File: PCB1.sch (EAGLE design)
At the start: 312 parts, among them SW1 CT10-XXXX-A2, SW10 CT10-XXXX-A2, SW100 CT10-XXXX-A2, SW101 CT10-XXXX-A2, SW102 CT10-XXXX-A2, SW103 CT10-XXXX-A2, SW104 CT10-XXXX-A2, SW105 CT10-XXXX-A2, SW106 CT10-XXXX-A2, SW107 CT10-XXXX-A2, SW108 CT10-XXXX-A2, SW109 CT10-XXXX-A2, SW11 CT10-XXXX-A2, SW110 CT10-XXXX-A2, SW111 CT10-XXXX-A2, SW112 CT10-XXXX-A2, SW113 CT10-XXXX-A2, SW114 CT10-XXXX-A2, SW115 CT10-XXXX-A2, SW116 CT10-XXXX-A2, SW117 CT10-XXXX-A2, SW118 CT10-XXXX-A2, SW119 CT10-XXXX-A2, SW12 CT10-XXXX-A2, SW120 CT10-XXXX-A2, SW121 CT10-XXXX-A2, SW122 CT10-XXXX-A2, SW123 CT10-XXXX-A2, SW124 CT10-XXXX-A2, SW125 CT10-XXXX-A2, SW126 CT10-XXXX-A2, SW127 CT10-XXXX-A2, SW128 CT10-XXXX-A2, SW129 CT10-XXXX-A2, SW13 CT10-XXXX-A2, SW130 CT10-XXXX-A2, SW131 CT10-XXXX-A2, SW132 CT10-XXXX-A2, SW14 CT10-XXXX-A2, SW15 CT10-XXXX-A2, SW16 CT10-XXXX-A2, SW17 CT10-XXXX-A2, SW18 CT10-XXXX-A2, SW19 CT10-XXXX-A2, SW2 CT10-XXXX-A2, SW20 CT10-XXXX-A2, SW21 CT10-XXXX-A2, SW22 CT10-XXXX-A2, SW23 CT10-XXXX-A2, SW24 CT10-XXXX-A2, SW25 CT10-XXXX-A2, SW26 CT10-XXXX-A2, SW27 CT10-XXXX-A2, SW28 CT10-XXXX-A2, SW29 CT10-XXXX-A2, SW3 CT10-XXXX-A2, SW30 CT10-XXXX-A2, SW31 CT10-XXXX-A2, SW32 CT10-XXXX-A2, SW33 CT10-XXXX-A2, SW34 CT10-XXXX-A2, SW35 CT10-XXXX-A2, SW36 CT10-XXXX-A2, SW37 CT10-XXXX-A2, SW38 CT10-XXXX-A2, SW39 CT10-XXXX-A2, SW4 CT10-XXXX-A2, SW40 CT10-XXXX-A2, SW41 CT10-XXXX-A2, SW42 CT10-XXXX-A2, SW43 CT10-XXXX-A2, SW44 CT10-XXXX-A2, SW45 CT10-XXXX-A2, SW46 CT10-XXXX-A2, SW47 CT10-XXXX-A2, SW48 CT10-XXXX-A2, SW49 CT10-XXXX-A2, SW5 CT10-XXXX-A2, SW50 CT10-XXXX-A2, SW51 CT10-XXXX-A2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

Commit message: updated schematic to include oscillator, resistor packages, and split main schematic into the five PCBs that we will need. Also started the PCB3 layout that includes the microcontroller.
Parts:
- removed C1, C2, C3, C4, C5, C6, C7: (no value), rcl:C-USC0805
- removed ICSP: (no value), pinhead:PINHD-2X3
- removed JP1, JP2, JP3, JP4: (no value), pinhead:PINHD-1X25
- removed LED100, LED101, LED102, LED103, LED104, LED105, LED106, LED107, LED108, LED109, LED110, LED111, LED112, LED113, LED114, LED115, LED116, LED117, LED118, LED119, LED120, LED121, LED122, LED123, LED124, LED125, LED126, LED127, LED128, LED129, LED130, LED131, LED132, LED133, LED134, LED135, LED136, LED137, LED138, LED139, LED20, LED21, LED22, LED23, LED24, LED25, LED32, LED33, LED34, LED35, LED36, LED37, LED38, LED39, LED40, LED41, LED42, LED43, LED44, LED45, LED46, LED47, LED48, LED49, LED50, LED51, LED52, LED53, LED54, LED55, LED56, LED57, LED58, LED59, LED60, LED61, LED62, LED63, LED64, LED65, LED66, LED67, LED68, LED69, LED70, LED71, LED72, LED73, LED74, LED75, LED76, LED77, LED78, LED79, LED80, LED81, LED82, LED83, LED84, LED85, LED86, LED87, LED88, LED89, LED90, LED91, LED92, LED93, LED94, LED95, LED96, LED97, LED98, LED99: (no value), led:LEDSMT1206
- removed SW1, SW10, SW100, SW101, SW102, SW103, SW104, SW105, SW106, SW107, SW108, SW109, SW11, SW110, SW111, SW112, SW113, SW114, SW115, SW116, SW117, SW118, SW119, SW12, SW120, SW121, SW122, SW123, SW124, SW125, SW126, SW127, SW128, SW129, SW13, SW130, SW131, SW132, SW14, SW15, SW16, SW17, SW18, SW19, SW2, SW20, SW21, SW22, SW23, SW24, SW25, SW26, SW27, SW28, SW29, SW3, SW30, SW31, SW32, SW33, SW34, SW35, SW36, SW37, SW38, SW39, SW4, SW40, SW41, SW42, SW43, SW44, SW45, SW46, SW47, SW48, SW49, SW5, SW50, SW51, SW52, SW53, SW54, SW55, SW56, SW57, SW58, SW59, SW6, SW60, SW61, SW62, SW63, SW64, SW65, SW66, SW67, SW68, SW69, SW7, SW70, SW71, SW72, SW73, SW74, SW75, SW76, SW77, SW78, SW79, SW8, SW80, SW81, SW82, SW83, SW84, SW85, SW86, SW87, SW88, SW89, SW9, SW90, SW91, SW92, SW93, SW94, SW95, SW96, SW97, SW98, SW99: CT10-XXXX-A2, switch-coto:CT10-XXXX-A2
- removed U$10, U$11, U$12, U$13, U$14, U$15, U$16, U$17, U$18, U$19, U$20, U$21, U$22, U$23, U$24, U$25, U$6, U$7, U$8, U$9: MM74HC595TSSOP-LD16, ECE477_Guitutar:MM74HC595TSSOP-LD16
- added R4, R5: (no value), resistor-bourns:4814P-T01
- R1, R2: device rcl:R-US_M0805 -> resistor-bourns:4814P-T01
- U$1: value PIC32MX570F512L -> MM74HC595TSSOP-LD16; device PICMX5xx:PIC32MX570F512L -> ECE477_Guitutar:MM74HC595TSSOP-LD16
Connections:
- removed net FRET1: JP2.16, SW1.2, SW2.2, SW3.2, SW4.2, SW5.2, SW6.2, U$1.AN12/PMA11/RB12
- removed net FRET10: JP3.2, SW55.2, SW56.2, SW57.2, SW58.2, SW59.2, SW60.2, U$1.AN38/RPF2/RF2
- removed net FRET11: JP3.3, SW61.2, SW62.2, SW63.2, SW64.2, SW65.2, SW66.2, U$1.AN39/RPF8/RF8
- removed net FRET12: JP3.8, SW67.2, SW68.2, SW69.2, SW70.2, SW71.2, SW72.2, U$1.SCL2/RA2
- removed net FRET13: JP3.9, SW73.2, SW74.2, SW75.2, SW76.2, SW77.2, SW78.2, U$1.SDA2/RA3
- removed net FRET14: JP3.10, SW79.2, SW80.2, SW81.2, SW82.2, SW83.2, SW84.2, U$1.TDI/CTED9/RA4
- removed net FRET15: JP3.11, SW85.2, SW86.2, SW87.2, SW88.2, SW89.2, SW90.2, U$1.TDO/RA5
- removed net FRET16: JP3.13, SW91.2, SW92.2, SW93.2, SW94.2, SW95.2, SW96.2, U$1.OSC1/CLKI/RC12
- removed net FRET17: JP3.14, SW100.2, SW101.2, SW102.2, SW97.2, SW98.2, SW99.2, U$1.OSC2/CLKO/RC15
- removed net FRET18: JP3.16, SW103.2, SW104.2, SW105.2, SW106.2, SW107.2, SW108.2, U$1.RPA14/SCL1/RA14
- removed net FRET19: JP3.17, SW109.2, SW110.2, SW111.2, SW112.2, SW113.2, SW114.2, U$1.RPA15/SDA1/RA15
- removed net FRET2: JP2.17, SW10.2, SW11.2, SW12.2, SW7.2, SW8.2, SW9.2, U$1.AN13/PMA10/RB13
- removed net FRET20: JP3.18, SW115.2, SW116.2, SW117.2, SW118.2, SW119.2, SW120.2, U$1.RPD8/RTCC/RD8
- removed net FRET21: JP3.19, SW121.2, SW122.2, SW123.2, SW124.2, SW125.2, SW126.2, U$1.RPD9/RD9
- removed net FRET22: JP3.20, SW127.2, SW128.2, SW129.2, SW130.2, SW131.2, SW132.2, U$1.RPD10/SCK1/PMA15/RD10
- removed net FRET3: JP2.18, SW13.2, SW14.2, SW15.2, SW16.2, SW17.2, SW18.2, U$1.AN14/RPB14/CTED5/PMA1/RB14
- removed net FRET4: JP2.19, SW19.2, SW20.2, SW21.2, SW22.2, SW23.2, SW24.2, U$1.AN15/RPB15/OCFB/CTED6/PMA0/RB15
- removed net FRET5: JP2.22, SW25.2, SW26.2, SW27.2, SW28.2, SW29.2, SW30.2, U$1.AN36/RPD14/RD14
- removed net FRET6: JP2.23, SW31.2, SW32.2, SW33.2, SW34.2, SW35.2, SW36.2, U$1.AN37/RPD15/SCK4/RD15
- removed net FRET7: JP2.24, SW37.2, SW38.2, SW39.2, SW40.2, SW41.2, SW42.2, U$1.RPF4/PMA9/RF4
- removed net FRET8: JP2.25, SW43.2, SW44.2, SW45.2, SW46.2, SW47.2, SW48.2, U$1.RPF5/PMA8/RF5
- removed net FRET9: JP3.1, SW49.2, SW50.2, SW51.2, SW52.2, SW53.2, SW54.2, U$1.USBID/RPF3/RF3
- removed net LED_SER10: JP4.16, U$1.RA6, U$12.SER
- removed net LED_SER11: JP4.15, U$1.RPG0/PMD8/RG0, U$13.SER
- removed net LED_SER12: JP4.14, U$1.RPG1/PMD9/RG1, U$14.SER
- removed net LED_SER13: JP4.13, U$1.AN45/RPF1/PMD10/RF1, U$15.SER
- removed net LED_SER14: JP4.12, U$1.AN44/C3INA/RPF0/PMD11/RF0, U$16.SER
- removed net LED_SER15: JP4.9, U$1.AN43/C3INB/PMD15/RD7, U$17.SER
- removed net LED_SER16: JP4.8, U$1.AN42/C3INC/PMD14/RD6, U$18.SER
- removed net LED_SER17: JP4.7, U$1.RPD5/PMRD/RD5, U$19.SER
- removed net LED_SER18: JP4.6, U$1.RPD4/PMWR/RD4, U$20.SER
- removed net LED_SER19: JP4.5, U$1.AN41/PMD13/RD13, U$21.SER
- removed net LED_SER20: JP4.4, U$1.AN40/RPD12/PMD12/RD12, U$22.SER
- removed net LED_SER21: JP4.3, U$1.AN26/C3IND/RPD3/RD3, U$23.SER
- removed net LED_SER22: JP4.2, U$1.AN25/RPD2/RD2, U$24.SER
- removed net LED_SER23: JP4.1, U$1.AN24/RPD1/RD1, U$25.SER
- removed net LED_SER5: JP4.21, U$1.RG12, U$7.SER
- removed net LED_SER6: JP4.20, U$1.RG14, U$8.SER
- removed net LED_SER7: JP4.19, U$1.AN47/PMD1/RE1, U$9.SER
- removed net LED_SER8: JP4.18, U$1.AN46/PMD0/RE0, U$10.SER
- removed net LED_SER9: JP4.17, U$1.CTED8/RA7, U$11.SER
- removed net N$107: LED34.A, U$8.QD
- removed net N$108: LED35.A, U$8.QE
- removed net N$109: LED33.A, U$8.QC
- removed net N$110: LED32.A, U$8.QB
- removed net N$111: LED36.A, U$8.QF
- removed net N$117: LED37.A, U$8.QA
- removed net N$118: LED40.A, U$9.QD
- removed net N$119: LED41.A, U$9.QE
- removed net N$120: LED39.A, U$9.QC
- removed net N$121: LED38.A, U$9.QB
- removed net N$122: LED42.A, U$9.QF
- removed net N$128: LED43.A, U$9.QA
- removed net N$129: LED46.A, U$10.QD
- removed net N$130: LED47.A, U$10.QE
- removed net N$131: LED45.A, U$10.QC
- removed net N$132: LED44.A, U$10.QB
- removed net N$133: LED48.A, U$10.QF
- removed net N$139: LED49.A, U$10.QA
- removed net N$140: LED52.A, U$11.QD
- removed net N$141: LED53.A, U$11.QE
- removed net N$142: LED51.A, U$11.QC
- removed net N$143: LED50.A, U$11.QB
- removed net N$144: LED54.A, U$11.QF
- removed net N$150: LED55.A, U$11.QA
- removed net N$151: LED58.A, U$12.QD
- removed net N$152: LED59.A, U$12.QE
- removed net N$153: LED57.A, U$12.QC
- removed net N$154: LED56.A, U$12.QB
- removed net N$155: LED60.A, U$12.QF
- removed net N$161: LED61.A, U$12.QA
- removed net N$162: LED64.A, U$13.QD
- removed net N$163: LED65.A, U$13.QE
- removed net N$164: LED63.A, U$13.QC
- removed net N$165: LED62.A, U$13.QB
- removed net N$166: LED66.A, U$13.QF
- removed net N$172: LED67.A, U$13.QA
- removed net N$173: LED70.A, U$14.QD
- removed net N$174: LED71.A, U$14.QE
- removed net N$175: LED69.A, U$14.QC
- removed net N$176: LED68.A, U$14.QB
- removed net N$177: LED72.A, U$14.QF
- removed net N$183: LED73.A, U$14.QA
- removed net N$184: LED76.A, U$15.QD
- removed net N$185: LED77.A, U$15.QE
- removed net N$186: LED75.A, U$15.QC
- removed net N$187: LED74.A, U$15.QB
- removed net N$188: LED78.A, U$15.QF
- removed net N$194: LED79.A, U$15.QA
- removed net N$195: LED82.A, U$16.QD
- removed net N$196: LED83.A, U$16.QE
- removed net N$197: LED81.A, U$16.QC
- removed net N$198: LED80.A, U$16.QB
- removed net N$199: LED84.A, U$16.QF
- removed net N$205: LED85.A, U$16.QA
- removed net N$206: LED88.A, U$17.QD
- removed net N$207: LED89.A, U$17.QE
- removed net N$208: LED87.A, U$17.QC
- removed net N$209: LED86.A, U$17.QB
- removed net N$210: LED90.A, U$17.QF
- removed net N$216: LED91.A, U$17.QA
- removed net N$217: LED94.A, U$18.QD
- removed net N$218: LED95.A, U$18.QE
- removed net N$219: LED93.A, U$18.QC
- removed net N$220: LED92.A, U$18.QB
- removed net N$221: LED96.A, U$18.QF
- removed net N$227: LED97.A, U$18.QA
- removed net N$228: LED100.A, U$19.QD
- removed net N$229: LED101.A, U$19.QE
- removed net N$230: LED99.A, U$19.QC
- removed net N$231: LED98.A, U$19.QB
- removed net N$232: LED102.A, U$19.QF
- removed net N$238: LED103.A, U$19.QA
- removed net N$239: LED106.A, U$20.QD
- removed net N$240: LED107.A, U$20.QE
- removed net N$241: LED105.A, U$20.QC
- removed net N$242: LED104.A, U$20.QB
- removed net N$243: LED108.A, U$20.QF
- removed net N$249: LED109.A, U$20.QA
- removed net N$250: LED112.A, U$21.QD
- removed net N$251: LED113.A, U$21.QE
- removed net N$252: LED111.A, U$21.QC
- removed net N$253: LED110.A, U$21.QB
- removed net N$254: LED114.A, U$21.QF
- removed net N$260: LED115.A, U$21.QA
- removed net N$261: LED118.A, U$22.QD
- removed net N$262: LED119.A, U$22.QE
- removed net N$263: LED117.A, U$22.QC
- removed net N$264: LED116.A, U$22.QB
- removed net N$265: LED120.A, U$22.QF
- removed net N$271: LED121.A, U$22.QA
- removed net N$272: LED124.A, U$23.QD
- removed net N$273: LED125.A, U$23.QE
- removed net N$274: LED123.A, U$23.QC
- removed net N$275: LED122.A, U$23.QB
- removed net N$276: LED126.A, U$23.QF
- removed net N$282: LED127.A, U$23.QA
- removed net N$283: LED130.A, U$24.QD
- removed net N$284: LED131.A, U$24.QE
- removed net N$285: LED129.A, U$24.QC
- removed net N$286: LED128.A, U$24.QB
- removed net N$287: LED132.A, U$24.QF
- removed net N$293: LED133.A, U$24.QA
- removed net N$294: LED136.A, U$25.QD
- removed net N$295: LED137.A, U$25.QE
- removed net N$296: LED135.A, U$25.QC
- removed net N$297: LED134.A, U$25.QB
- removed net N$298: LED138.A, U$25.QF
- removed net N$304: LED139.A, U$25.QA
- removed net N$42: JP2.1, U$1.PGEC2/AN6/RPB6/RB6
- removed net N$45: JP2.4, U$1.VREF+/PMA6/RA10
- removed net N$52: JP2.13, U$1.TCK/CTED2/RA1
- removed net N$55: LED22.A, U$6.QD
- removed net N$56: LED23.A, U$6.QE
- removed net N$57: LED21.A, U$6.QC
- removed net N$58: LED20.A, U$6.QB
- removed net N$59: LED24.A, U$6.QF
- removed net N$65: LED25.A, U$6.QA
- removed net N$73: LED30.A, U$7.QF
- removed net N$79: LED31.A, U$7.QA
- removed net RCK: JP3.23, U$1.SOSCI/RPC13/RC13, U$10.RCK, U$11.RCK, U$12.RCK, U$13.RCK, U$14.RCK, U$15.RCK, U$16.RCK, U$17.RCK, U$18.RCK, U$19.RCK, U$20.RCK, U$21.RCK, U$22.RCK, U$23.RCK, U$24.RCK, U$25.RCK, U$3.RCK, U$4.RCK, U$5.RCK, U$6.RCK, U$7.RCK, U$8.RCK, U$9.RCK
- removed net SCK: JP3.22, U$1.RPD0/INT0/RD0, U$10.SCK, U$11.SCK, U$12.SCK, U$13.SCK, U$14.SCK, U$15.SCK, U$16.SCK, U$17.SCK, U$18.SCK, U$19.SCK, U$20.SCK, U$21.SCK, U$22.SCK, U$23.SCK, U$24.SCK, U$25.SCK, U$3.SCK, U$4.SCK, U$5.SCK, U$6.SCK, U$7.SCK, U$8.SCK, U$9.SCK
- removed net SCLR: JP3.21, U$1.RPD11/PMA14/RD11, U$10.SCLR, U$11.SCLR, U$12.SCLR, U$13.SCLR, U$14.SCLR, U$15.SCLR, U$16.SCLR, U$17.SCLR, U$18.SCLR, U$19.SCLR, U$20.SCLR, U$21.SCLR, U$22.SCLR, U$23.SCLR, U$24.SCLR, U$25.SCLR, U$3.SCLR, U$4.SCLR, U$5.SCLR, U$6.SCLR, U$7.SCLR, U$8.SCLR, U$9.SCLR
- removed net STRING1: JP2.7, SW1.1, SW102.1, SW108.1, SW114.1, SW12.1, SW120.1, SW126.1, SW132.1, SW18.1, SW24.1, SW30.1, SW36.1, SW42.1, SW48.1, SW54.1, SW60.1, SW66.1, SW72.1, SW78.1, SW84.1, SW90.1, SW96.1, U$1.AN8/RPB8/CTED10/RB8
- removed net STRING2: JP2.8, SW103.1, SW109.1, SW115.1, SW121.1, SW127.1, SW13.1, SW19.1, SW2.1, SW25.1, SW31.1, SW37.1, SW43.1, SW49.1, SW55.1, SW61.1, SW67.1, SW7.1, SW73.1, SW79.1, SW85.1, SW91.1, SW97.1, U$1.AN9/RPB9/CTED4/RB9
- removed net STRING3: JP2.9, SW104.1, SW110.1, SW116.1, SW122.1, SW128.1, SW14.1, SW20.1, SW26.1, SW3.1, SW32.1, SW38.1, SW44.1, SW50.1, SW56.1, SW62.1, SW68.1, SW74.1, SW8.1, SW80.1, SW86.1, SW92.1, SW98.1, U$1.CVREFOUT/AN10/RPB10/CTED11/PMA13/RB10
- removed net STRING4: JP2.10, SW105.1, SW111.1, SW117.1, SW123.1, SW129.1, SW15.1, SW21.1, SW27.1, SW33.1, SW39.1, SW4.1, SW45.1, SW51.1, SW57.1, SW63.1, SW69.1, SW75.1, SW81.1, SW87.1, SW9.1, SW93.1, SW99.1, U$1.AN11/PMA12/RB11
- removed net STRING5: JP2.14, SW10.1, SW100.1, SW106.1, SW112.1, SW118.1, SW124.1, SW130.1, SW16.1, SW22.1, SW28.1, SW34.1, SW40.1, SW46.1, SW5.1, SW52.1, SW58.1, SW64.1, SW70.1, SW76.1, SW82.1, SW88.1, SW94.1, U$1.AN34/RPF13/SCK3/RF13
- removed net STRING6: JP2.15, SW101.1, SW107.1, SW11.1, SW113.1, SW119.1, SW125.1, SW131.1, SW17.1, SW23.1, SW29.1, SW35.1, SW41.1, SW47.1, SW53.1, SW59.1, SW6.1, SW65.1, SW71.1, SW77.1, SW83.1, SW89.1, SW95.1, U$1.AN35/RPF12/RF12
- removed net VSS: C2.1, C3.2, C4.2, C5.1, C6.2, JP1.15, JP2.20, JP2.6, JP3.15, JP3.25, U$1.AVSS, U$1.VSS1, U$1.VSS3, U$1.VSS4, U$1.VSS5
- new net N$20: R2.12, U$1.QC
- new net N$21: R2.11, U$1.QD
- new net N$22: R2.10, U$1.QE
- new net N$23: R2.9, U$1.QF
- new net N$24: R2.14, U$1.QA
- new net N$25: LED13.A, R2.1
- new net N$31: U$3.G
- new net N$33: U$3.SCK
- new net N$34: U$3.RCK
- new net N$35: R4.13, U$3.QB
- new net N$46: LED16.A, R4.4
- new net N$47: LED17.A, R4.5
- new net N$48: U$4.SCK
- new net N$49: LED18.A, R4.6
- new net N$53: U$5.SCK
- new net N$60: R5.13, U$5.QB
- new net N$61: R5.12, U$5.QC
- new net N$62: R5.11, U$5.QD
- new net N$63: R5.10, U$5.QE
- new net N$64: R5.9, U$5.QF
- net G: no longer JP3.24, U$1.SOSCO/RPC14/T1CK/RC14, U$10.G, U$11.G, U$12.G, U$13.G, U$14.G, U$15.G, U$16.G, U$17.G, U$18.G, U$19.G, U$20.G, U$21.G, U$22.G, U$23.G, U$24.G, U$25.G, U$3.G, U$5.G, U$6.G, U$7.G, U$8.G, U$9.G
- net GND: now also U$1.GND; no longer LED100.C, LED101.C, LED102.C, LED103.C, LED104.C, LED105.C, LED106.C, LED107.C, LED108.C, LED109.C, LED110.C, LED111.C, LED112.C, LED113.C, LED114.C, LED115.C, LED116.C, LED117.C, LED118.C, LED119.C, LED120.C, LED121.C, LED122.C, LED123.C, LED124.C, LED125.C, LED126.C, LED127.C, LED128.C, LED129.C, LED130.C, LED131.C, LED132.C, LED133.C, LED134.C, LED135.C, LED136.C, LED137.C, LED138.C, LED139.C, LED20.C, LED21.C, LED22.C, LED23.C, LED24.C, LED25.C, LED32.C, LED33.C, LED34.C, LED35.C, LED36.C, LED37.C, LED38.C, LED39.C, LED40.C, LED41.C, LED42.C, LED43.C, LED44.C, LED45.C, LED46.C, LED47.C, LED48.C, LED49.C, LED50.C, LED51.C, LED52.C, LED53.C, LED54.C, LED55.C, LED56.C, LED57.C, LED58.C, LED59.C, LED60.C, LED61.C, LED62.C, LED63.C, LED64.C, LED65.C, LED66.C, LED67.C, LED68.C, LED69.C, LED70.C, LED71.C, LED72.C, LED73.C, LED74.C, LED75.C, LED76.C, LED77.C, LED78.C, LED79.C, LED80.C, LED81.C, LED82.C, LED83.C, LED84.C, LED85.C, LED86.C, LED87.C, LED88.C, LED89.C, LED90.C, LED91.C, LED92.C, LED93.C, LED94.C, LED95.C, LED96.C, LED97.C, LED98.C, LED99.C, U$10.GND, U$11.GND, U$12.GND, U$13.GND, U$14.GND, U$15.GND, U$16.GND, U$17.GND, U$18.GND, U$19.GND, U$20.GND, U$21.GND, U$22.GND, U$23.GND, U$24.GND, U$25.GND, U$6.GND, U$7.GND, U$8.GND, U$9.GND
- net LED_SER1: now also U$4.SER; no longer JP4.25, U$1.AN21/PMD4/RE4, U$3.SER
- net LED_SER2: now also U$1.SER; no longer JP4.24, U$1.RPE3/CTPLS/PMD3/RE3, U$4.SER
- net LED_SER3: now also U$3.SER; no longer JP4.23, U$1.AN20/PMD2/RE2, U$5.SER
- net LED_SER4: now also U$5.SER; no longer JP4.22, U$1.RG13, U$6.SER
- net N$1: now also R1.13, U$4.QB; no longer C1.1, R1.1, R2.1
- net N$10: now also LED4.A, R1.4; no longer C6.1, JP4.11, U$1.VDD5
- net N$11: now also R1.5; no longer U$3.QE
- net N$12: now also LED6.A, R1.6; no longer C7.2, JP4.10, U$1.VCAP
- net N$13: now also U$1.G; no longer ICSP.1, JP1.13, R1.2, U$1.MCLR
- net N$14: now also U$1.SCLR, U$3.SCLR, U$4.SCLR, U$5.SCLR; no longer ICSP.4, JP1.25, U$1.PGED1/AN0/RPB0/RB0
- net N$17: now also U$1.SCK; no longer LED3.A, U$3.QC
- net N$18: now also U$1.RCK; no longer LED2.A, U$3.QB
- net N$19: now also R2.13, U$1.QB; no longer LED6.A, U$3.QF
- net N$2: now also R1.12, U$4.QC; no longer ICSP.5, JP1.24, U$1.PGEC1/AN1/RPB1/CTED12/RB1
- net N$26: now also LED8.A, R2.2; no longer LED10.A, U$4.QD
- net N$27: now also LED9.A, R2.3; no longer LED11.A, U$4.QE
- net N$28: now also LED10.A, R2.4; no longer LED9.A, U$4.QC
- net N$29: now also LED11.A, R2.5; no longer LED8.A, U$4.QB
- net N$3: now also R1.11, U$4.QD; no longer JP1.17, U$1.TMS/CTED1/RA0
- net N$30: now also R2.6; no longer U$4.QF
- net N$36: now also R4.12, U$3.QC; no longer LED13.A, U$4.QA
- net N$37: now also R4.11, U$3.QD; no longer LED16.A, U$5.QD
- net N$38: now also R4.10, U$3.QE; no longer LED17.A, U$5.QE
- net N$39: now also R4.9, U$3.QF; no longer LED15.A, U$5.QC
- net N$4: now also R1.10, U$4.QE; no longer JP1.22, U$1.PGED3/AN3/C2INA/RPB3/RB3
- net N$40: now also R4.14, U$3.QA; no longer LED14.A, U$5.QB
- net N$41: now also LED19.A, R4.1; no longer LED18.A, U$5.QF
- net N$43: now also LED14.A, R4.2; no longer JP2.2, U$1.PGED2/AN7/RPB7/CTED3/RB7
- net N$44: now also LED15.A, R4.3; no longer JP2.3, U$1.VREF-/PMA7/RA9
- net N$5: now also R1.9, U$4.QF; no longer JP1.23, U$1.PGEC3/AN2/CTCMP/C2INB/RPB2/CTED13/RB2
- net N$50: now also U$5.G; no longer JP2.11, U$1.VSS2
- net N$51: now also U$4.RCK; no longer JP2.12, U$1.VDD2
- net N$54: now also U$5.RCK; no longer LED19.A, U$5.QA
- net N$6: now also R1.1; no longer U$3.QA
- net N$66: now also R5.14, U$5.QA; no longer JP3.4, U$1.VBUS
- net N$67: now also LED31.A, R5.1; no longer JP3.6, U$1.D-
- net N$68: now also LED26.A, R5.2; no longer JP3.7, U$1.D+
- net N$69: now also LED27.A, R5.3; no longer LED28.A, U$7.QD
- net N$7: now also R1.14, U$4.QA; no longer C4.1, JP2.21, U$1.VDD3
- net N$70: now also LED28.A, R5.4; no longer LED29.A, U$7.QE
- net N$71: now also LED29.A, R5.5; no longer LED27.A, U$7.QC
- net N$72: now also LED30.A, R5.6; no longer LED26.A, U$7.QB
- net N$8: now also LED2.A, R1.2; no longer LED4.A, U$3.QD
- net N$9: now also LED3.A, R1.3; no longer C5.2, JP3.12, JP3.5, U$1.VDD4, U$1.VUSB3V3
- net P0_0: no longer JP1.14, JP1.18, U$1.AN19/C2INC/RPG9/PMA2/RG9, U$1.AN32/RPE8/RE8
- net P0_4: no longer JP1.3, U$1.AN22/RPE5/PMD5/RE5
- net P0_5: no longer JP1.12, U$1.AN18/C2IND/RPG8/PMA3/RG8
- net P1_5: no longer JP1.1, U$1.AN28/RG15
- net P1_7: no longer JP1.19, U$1.AN33/RPE9/RE9
- net P3_1: no longer JP1.11, U$1.AN17/C1INC/RPG7/PMA4/RG7
- net P3_2: no longer JP1.10, U$1.AN16/C1IND/RPG6/SCK2/PMA5/RG6
- net P3_3: no longer JP1.9, U$1.RPC4/CTED7/RC4
- net P3_4: no longer JP1.8, U$1.AN31/RPC3/RC3
- net P3_7: no longer JP1.7, U$1.AN30/RPC2/RC2
- net PE: no longer C1.2, C7.1
- net RST_N: no longer JP1.6, U$1.AN29/RPC1/RC1
- net RXD: no longer JP1.21, U$1.AN4/C1INB/RB4
- net SW_BTN: no longer JP1.4, U$1.AN23/PMD6/RE6
- net TXD: no longer JP1.20, U$1.AN5/C1INA/RPB5/VBUSON/RB5
- net VCC: now also U$1.VCC; no longer U$10.VCC, U$11.VCC, U$12.VCC, U$13.VCC, U$14.VCC, U$15.VCC, U$16.VCC, U$17.VCC, U$18.VCC, U$19.VCC, U$20.VCC, U$21.VCC, U$22.VCC, U$23.VCC, U$24.VCC, U$25.VCC, U$6.VCC, U$7.VCC, U$8.VCC, U$9.VCC
- net VDD: no longer C2.2, C3.1, JP1.16, JP1.2, JP2.5, R2.2, U$1.AVDD, U$1.VDD, U$1.VDD1
- net WAKEUP: no longer JP1.5, U$1.AN27/PMD7/RE7

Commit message: Started PCB1 layout. Added pads for fret. Updated BT module to SPPS5.
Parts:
- added PAD1, PAD2: WIREPAD2,54/0,9, wirepad:WIREPAD2,54/0,9
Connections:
- removed net N$13: U$1.G
- removed net N$17: U$1.SCK
- removed net N$18: U$1.RCK
- removed net N$31: U$3.G
- removed net N$33: U$3.SCK
- removed net N$34: U$3.RCK
- removed net N$50: U$5.G
- removed net N$53: U$5.SCK
- removed net N$54: U$5.RCK
- removed net PE: C8.2, U$2.GND, U$2.GND1
- new net FRET1: PAD1.P
- new net FRET2: PAD2.P
- net G: now also U$1.G, U$3.G, U$5.G
- net GND: now also C8.2, U$2.GN2, U$2.GND, U$2.GND1, U$2.GND3, U$2.GND4, U$2.GND5
- net LED: now also U$2.LED; no longer U$2.LED1
- net N$48: now also U$1.SCK, U$3.SCK, U$5.SCK
- net N$51: now also U$1.RCK, U$3.RCK, U$5.RCK
- net P0_0: now also U$2.P0_0/RTS; no longer U$2.P0_0
- net P1_7: now also U$2.P1_7/CTS; no longer U$2.P1_7
- net RXD: now also U$2.RXD; no longer U$2.HCI_RXD
- net TXD: now also U$2.TXD; no longer U$2.HCI_TXD

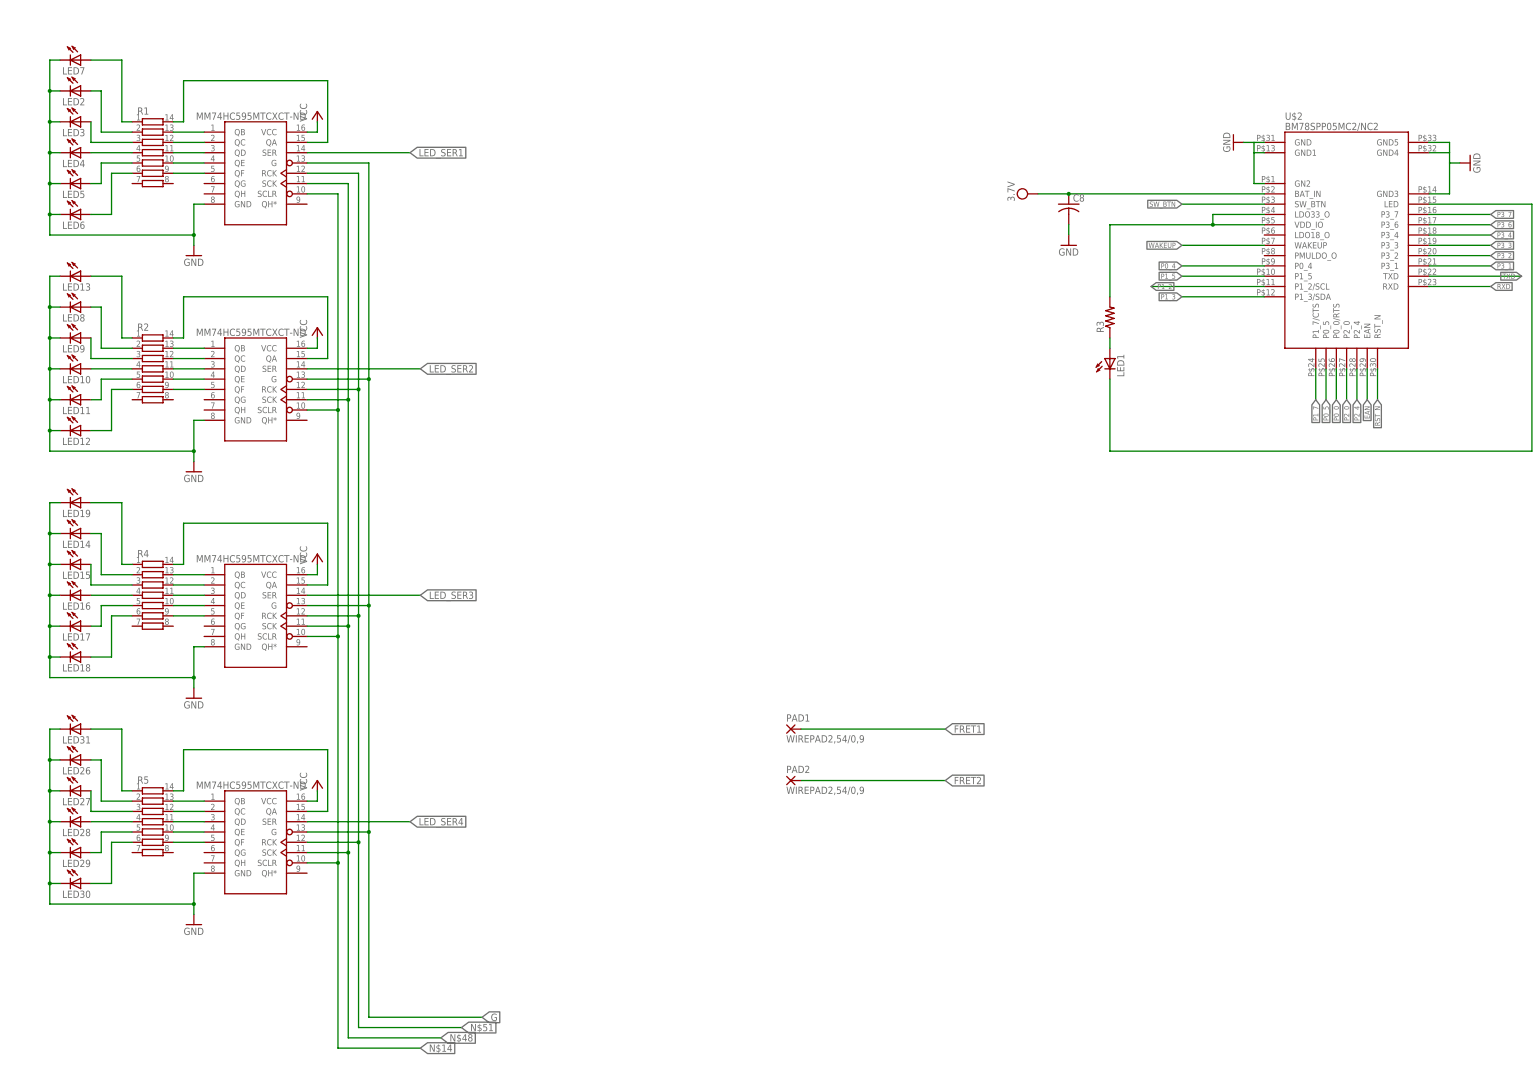
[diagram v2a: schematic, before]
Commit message: Progress on PCB1 layout. Added solder jumpers to schematic.
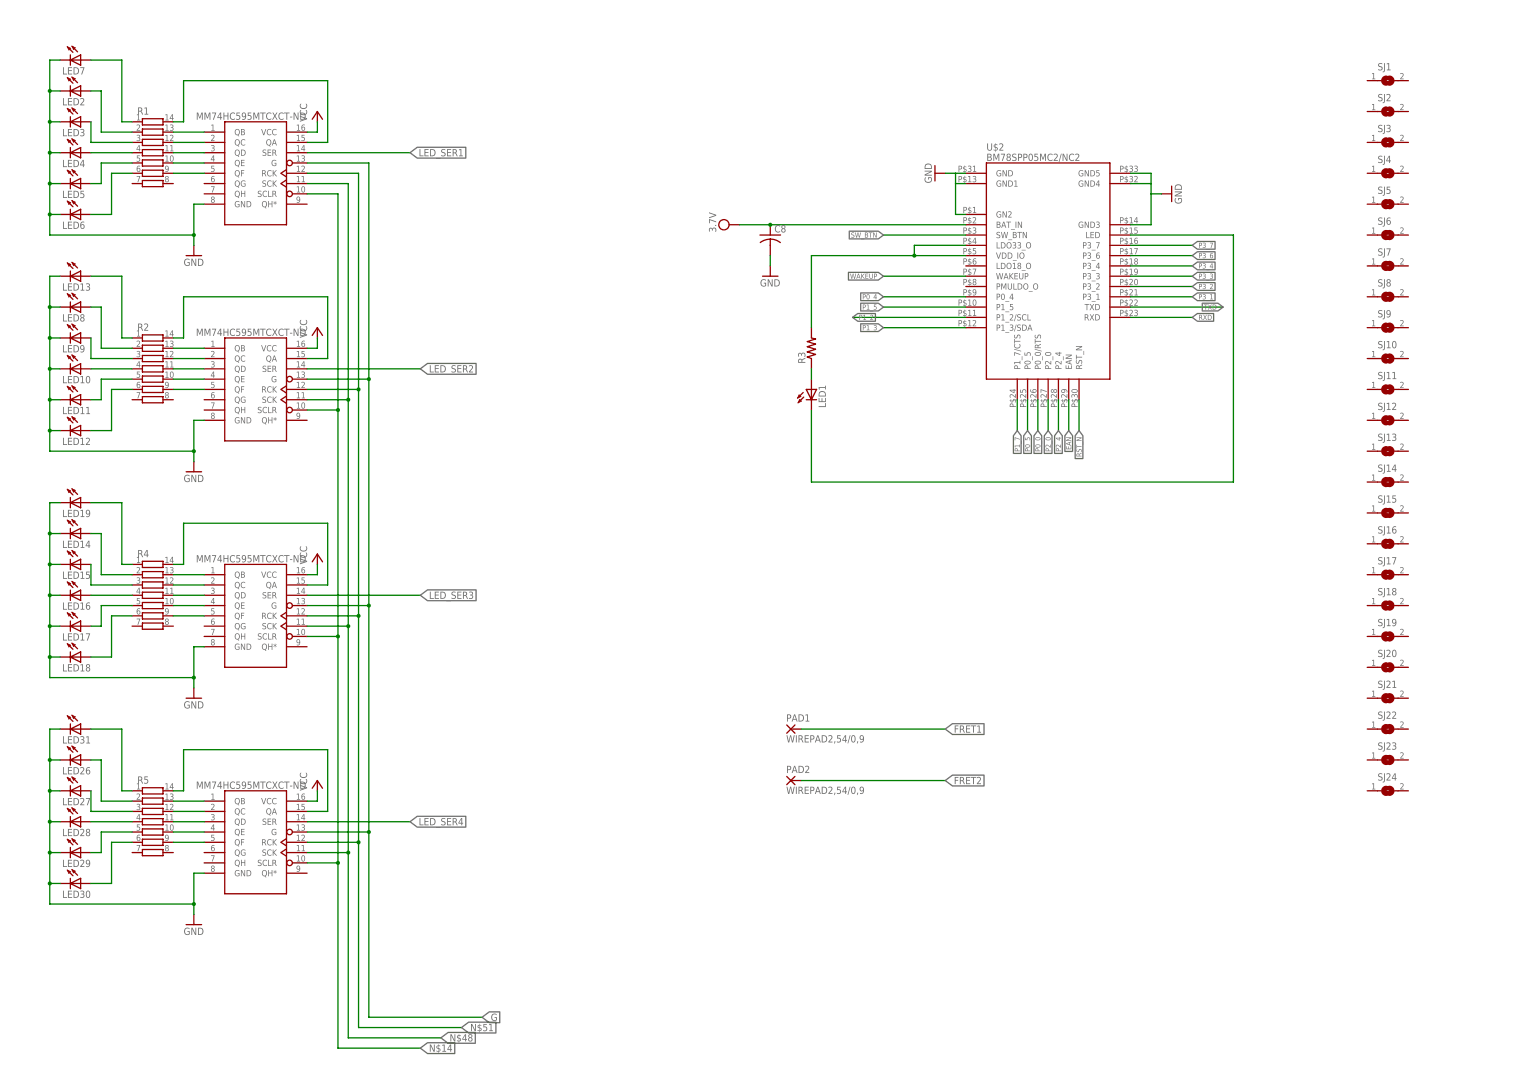
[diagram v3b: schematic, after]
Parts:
- added SJ1, SJ10, SJ11, SJ12, SJ13, SJ14, SJ15, SJ16, SJ17, SJ18, SJ19, SJ2, SJ20, SJ21, SJ22, SJ23, SJ24, SJ3, SJ4, SJ5, SJ6, SJ7, SJ8, SJ9: (no value), jumper:SJ
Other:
- moved on the sheet: C8, LED1, R3, U$2

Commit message: Finished PCB1, PCB3, and added parts to ECE477 library
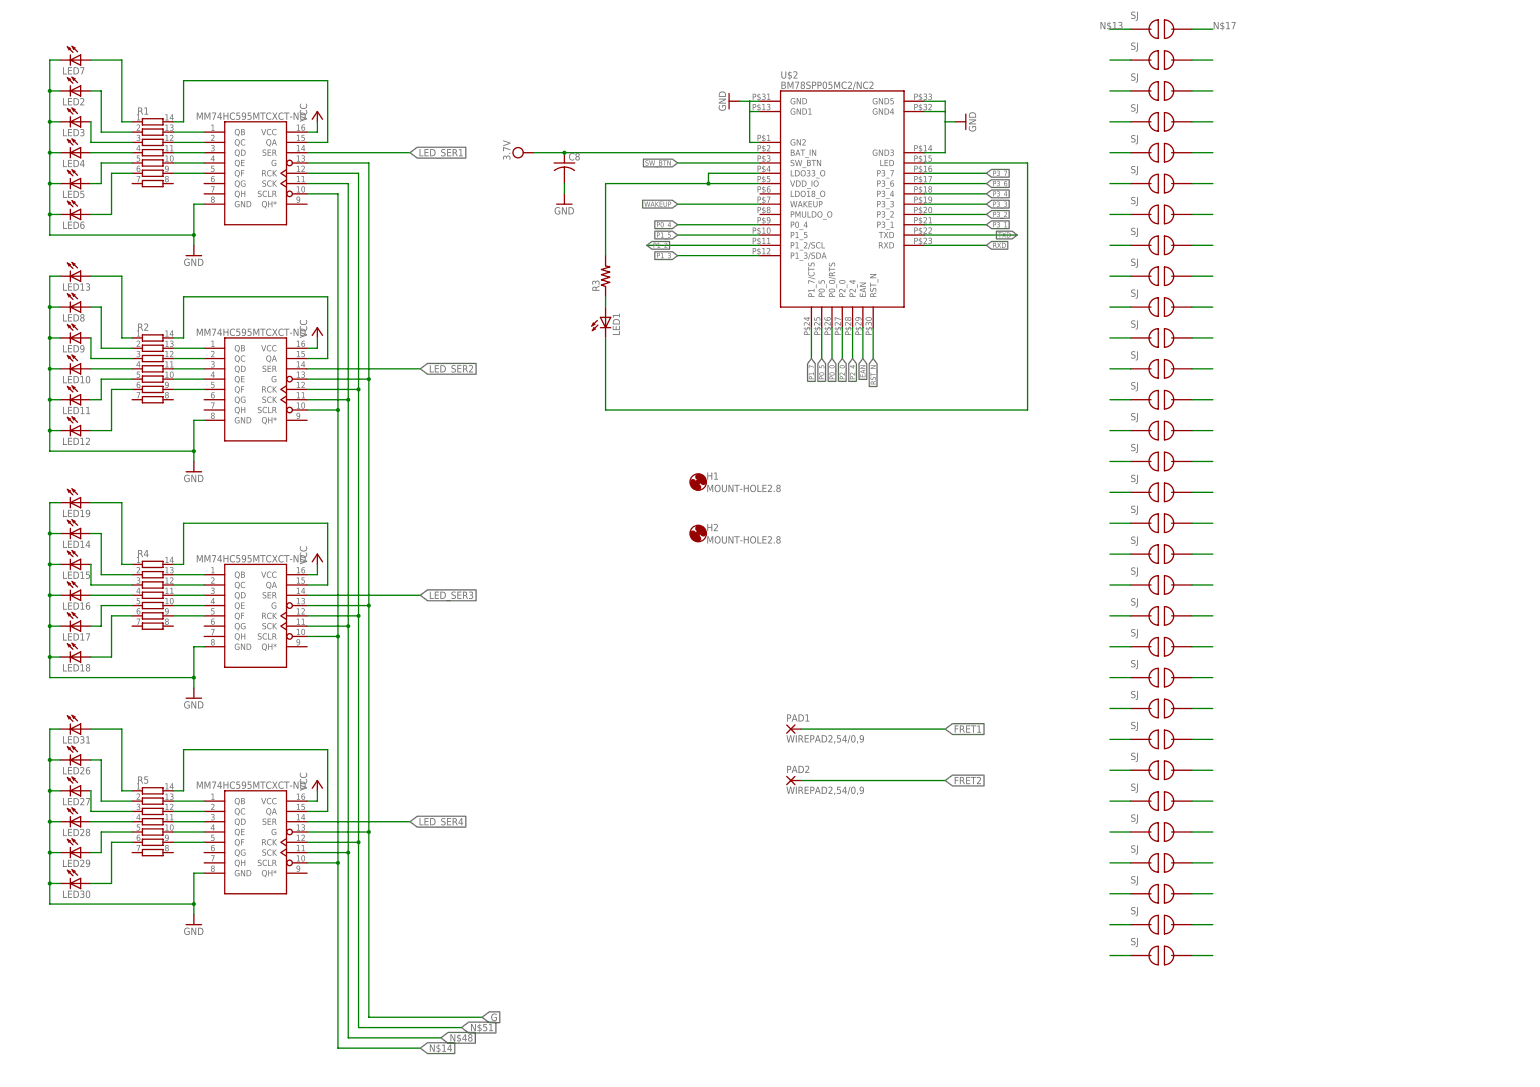
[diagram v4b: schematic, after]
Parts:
- removed SJ1, SJ10, SJ11, SJ12, SJ13, SJ14, SJ15, SJ16, SJ17, SJ18, SJ19, SJ2, SJ20, SJ21, SJ22, SJ23, SJ24, SJ3, SJ4, SJ5, SJ6, SJ7, SJ8, SJ9: (no value), jumper:SJ
- added H1, H2: MOUNT-HOLE2.8, holes:MOUNT-HOLE2.8
- added U$10, U$11, U$12, U$13, U$14, U$15, U$16, U$17, U$18, U$19, U$20, U$21, U$22, U$23, U$24, U$25, U$26, U$27, U$28, U$29, U$30, U$31, U$32, U$33, U$34, U$35, U$36, U$6, U$7, U$8, U$9: JUMPER, ECE477_Guitutar:JUMPER
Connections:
- new net N$100: U$31.P$1
- new net N$101: U$30.P$1
- new net N$102: U$29.P$1
- new net N$103: U$28.P$1
- new net N$104: U$27.P$1
- new net N$105: U$26.P$1
- new net N$106: U$25.P$1
- new net N$107: U$24.P$1
- new net N$108: U$23.P$1
- new net N$109: U$22.P$1
- new net N$110: U$21.P$1
- new net N$111: U$20.P$1
- new net N$112: U$19.P$1
- new net N$113: U$18.P$1
- new net N$114: U$17.P$1
- new net N$115: U$16.P$1
- new net N$13: U$35.P$1
- new net N$17: U$35.P$2
- new net N$18: U$34.P$1
- new net N$31: U$34.P$2
- new net N$32: U$33.P$2
- new net N$33: U$33.P$1
- new net N$34: U$6.P$1
- new net N$42: U$7.P$1
- new net N$45: U$8.P$1
- new net N$50: U$9.P$1
- new net N$52: U$6.P$2
- new net N$53: U$7.P$2
- new net N$54: U$8.P$2
- new net N$55: U$9.P$2
- new net N$56: U$10.P$1
- new net N$57: U$11.P$1
- new net N$58: U$10.P$2
- new net N$59: U$11.P$2
- new net N$65: U$12.P$2
- new net N$73: U$12.P$1
- new net N$74: U$13.P$1
- new net N$75: U$13.P$2
- new net N$76: U$14.P$2
- new net N$77: U$14.P$1
- new net N$78: U$15.P$1
- new net N$79: U$15.P$2
- new net N$80: U$16.P$2
- new net N$81: U$17.P$2
- new net N$82: U$18.P$2
- new net N$83: U$19.P$2
- new net N$84: U$20.P$2
- new net N$85: U$21.P$2
- new net N$86: U$22.P$2
- new net N$87: U$23.P$2
- new net N$88: U$24.P$2
- new net N$89: U$25.P$2
- new net N$90: U$26.P$2
- new net N$91: U$27.P$2
- new net N$92: U$28.P$2
- new net N$93: U$29.P$2
- new net N$94: U$30.P$2
- new net N$95: U$31.P$2
- new net N$96: U$32.P$2
- new net N$97: U$36.P$2
- new net N$98: U$36.P$1
- new net N$99: U$32.P$1
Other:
- moved on the sheet: C8, LED1, R3, U$2

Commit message: Finished changing dimensions for PCB3 and switched out resistors for smaller ones.
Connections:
- net N$14 renamed SCLR
- net N$48 renamed SCK
- net N$51 renamed RCK
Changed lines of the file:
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@@
 <?xml version="1.0" encoding="utf-8"?>
 <!DOCTYPE eagle SYSTEM "eagle.dtd">
-<eagle version="8.0.0">
+<eagle version="8.0.1">
 <drawing>
 <settings>
@@
 </segment>
 </net>
-<net name="N$48" class="0">
+<net name="SCK" class="0">
 <segment>
 <wire x1="96.52" y1="231.14" x2="96.52" y2="177.8" width="0.1524" layer="91"/>
@@
 </segment>
 </net>
-<net name="N$51" class="0">
+<net name="RCK" class="0">
 <segment>
 <wire x1="99.06" y1="233.68" x2="99.06" y2="180.34" width="0.1524" layer="91"/>
@@
 </segment>
 </net>
-<net name="N$14" class="0">
+<net name="SCLR" class="0">
 <segment>
 <wire x1="86.36" y1="228.6" x2="93.98" y2="228.6" width="0.1524" layer="91"/>
